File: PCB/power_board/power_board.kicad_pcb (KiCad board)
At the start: 4 copper layers, 70 x 70 mm, 76 parts, among them IC1 TPS6213013AQRGTTQ1, IC10 LSM6DSV16BXTR, IC11 TPS61032PWP, IC7 BQ51013BRHLR, IC8 TPS63000IDRCRQ1, IC9 MAX17048G+T10, J1 Speaker_con, J2 DS1013-40SSIB1-B-0, J8 UJ20-C-H-G-MSMT-R-4C-P16-TR, J9 QVAR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

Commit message: everything checked
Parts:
- added H1: MountingHole, MountingHole:MountingHole_3.2mm_M3_Pad_Via, F.Cu at (32.4, 103.0)
- added H2: MountingHole, MountingHole:MountingHole_3.2mm_M3_Pad_Via, F.Cu at (96.7, 103.5)
- added H3: MountingHole, MountingHole:MountingHole_3.2mm_M3_Pad_Via, F.Cu at (32.6, 167.7)
- added H4: MountingHole, MountingHole:MountingHole_3.2mm_M3_Pad_Via, F.Cu at (97.0, 167.7)
- moved R39 3.66 mm to (30.4, 107.6)
- moved J8 2.58 mm to (44.1, 166.8)
- renumbered indukcja1 to indukcja
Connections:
- D8 pad 4: /USB_D- -> /USB_D-_S
- D8 pad 6: /USB_D+ -> /USB_D+_S
- J2 pad 37: /USB_D+ -> /USB_D+_S
- J2 pad 39: /USB_D- -> /USB_D-_S
- J2 pad 40: unconnected-(J2-Pad40) -> GND
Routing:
- net /USB_D-_S: track 0.00 -> 15.2 mm, vias 0 -> 1
- net /USB_D+_S: track 0.00 -> 15.1 mm
- net /USB_D+: track 29.4 -> 19.0 mm
- net /USB_D-: track 35.6 -> 25.4 mm, vias 3 -> 2
- net GND: track 89.6 -> 93.0 mm
- net Net-(D7-A): track 74.1 -> 77.0 mm
- net Net-(J8-CC1): track 28.4 -> 31.2 mm
- net Net-(J8-CC2): track 11.8 -> 13.7 mm
- net /V_SYS: track 136.9 -> 136.1 mm
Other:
- board size 70 x 70 mm -> 73 x 73 mm

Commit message: all my pcb
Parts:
- removed J8: UJ20-C-H-G-MSMT-R-4C-P16-TR, UJ20-C-H-G-MSMT-R-4C-P16-TR:UJ20CHGMSMTR4CP16TR
- removed J9: QVAR, Connector_JST:JST_PH_B3B-PH-K_1x03_P2.00mm_Vertical
- removed indukcja: Conn_01x02, Connector_PinHeader_2.54mm:PinHeader_1x02_P2.54mm_Vertical
- added J3: USB4110GFA, USB4110GFA:GCT_USB4110GFA, F.Cu at (44.1, 165.2)
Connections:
- net Net-(D7-A) renamed VBUS
- IC10 pad 6: Net-(IC10-AH1/QVAR1) -> unconnected-(IC10-AH1/QVAR1-Pad6)
- IC10 pad 9: Net-(IC10-AH2/QVAR2) -> unconnected-(IC10-AH2/QVAR2-Pad9)
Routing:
- net GND: track 93.0 -> 108.5 mm, vias 33 -> 36
- net Net-(IC10-AH1/QVAR1): track 15.0 -> 0.00 mm, vias 1 -> 0
- net Net-(IC10-AH2/QVAR2): track 9.12 -> 0.00 mm
- net /Movement/WCLK: track 20.4 -> 22.8 mm
- net /USB_D+: track 19.0 -> 21.3 mm
- net VBUS: track 77.0 -> 79.3 mm
- net /USB_D-: track 25.4 -> 27.6 mm
- net /Movement/IMU_INT2: track 14.8 -> 16.8 mm
- net Net-(J3-CC2): track 13.7 -> 14.9 mm
- net Net-(J3-CC1): track 31.2 -> 32.4 mm
- net unconnected-(IC10-AH1/QVAR1-Pad6): track 0.00 -> 0.95 mm, vias 0 -> 1

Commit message: imu from board
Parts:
- removed IC10: LSM6DSV16BXTR, LSM6DSV16BXTR:LSM6DSV16BXTR
- added J4: IMU_connector, Connector_PinHeader_2.54mm:PinHeader_2x05_P2.54mm_Vertical, F.Cu at (73.3, 111.6)
- moved C2 1.35 mm to (78.3, 107.7)
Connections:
- J2 pad 16: /Movement/DATA_IN -> /Movement/SCX
- J2 pad 18: /Movement/BCLK -> /Movement/SDX
- J2 pad 26: /Movement/WCLK -> unconnected-(J2-Pad26)
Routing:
- net /Movement/VOUT_3V3: track 149.9 -> 114.2 mm, vias 3 -> 1
- net /Movement/SDX: track 0.00 -> 24.8 mm
- net /Movement/WCLK: track 22.8 -> 0.00 mm, vias 1 -> 0
- net /Movement/SCX: track 0.00 -> 17.1 mm
- net /Movement/MISO: track 41.8 -> 33.0 mm, vias 3 -> 2
- net /Movement/BCLK: track 8.55 -> 0.00 mm
- net /Movement/DATA_IN: track 7.28 -> 0.00 mm
- net GND: track 108.5 -> 101.9 mm, vias 36 -> 37
- net /Movement/IMU_INT2: track 16.8 -> 10.2 mm, vias 1 -> 0
- net /Movement/MOSI: track 37.6 -> 32.6 mm, vias 3 -> 1
- net /Movement/IMU_CS: track 11.6 -> 8.62 mm, vias 2 -> 0
- net Net-(IC8-VINA): track 23.0 -> 21.7 mm, vias 1 -> 0
- net unconnected-(IC10-AH1/QVAR1-Pad6): track 0.95 -> 0.00 mm, vias 1 -> 0
- net /Movement/SCLK: track 47.3 -> 48.0 mm
- net /Movement/IMU_INT1: track 11.0 -> 11.2 mm, vias 1 -> 0

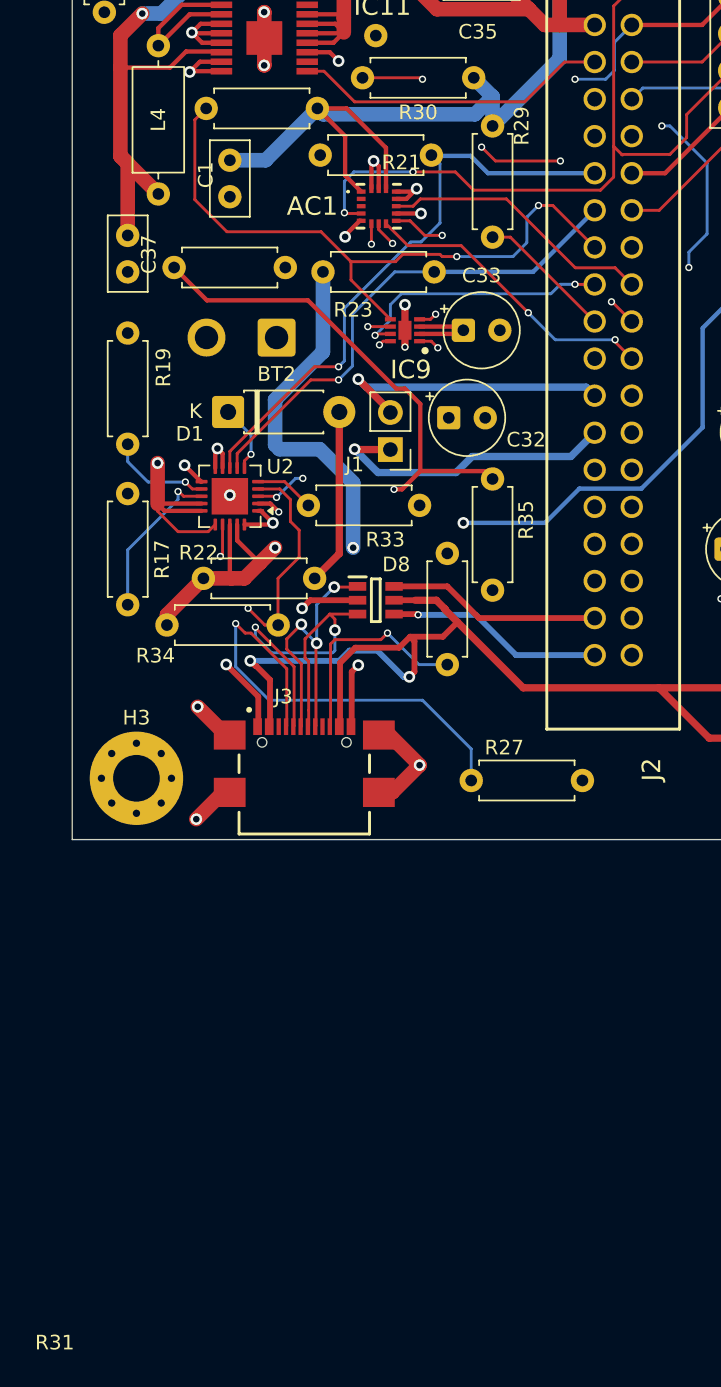
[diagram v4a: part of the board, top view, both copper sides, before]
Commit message: accel changed to goldpin
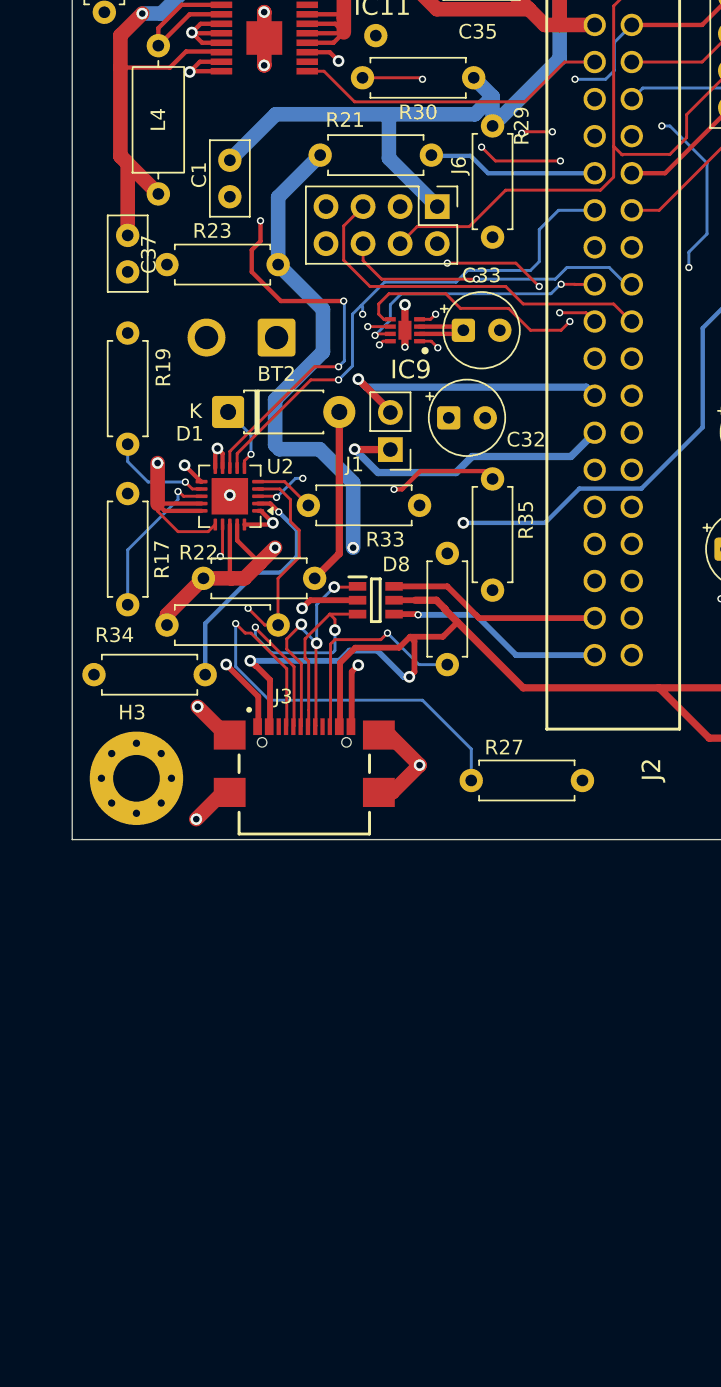
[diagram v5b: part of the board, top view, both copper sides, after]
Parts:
- removed AC1: H3LIS331DLTR, H3LIS331DLTR:LIS3DHTR
- removed R31: 100kΩ, Resistor_THT:R_Axial_DIN0207_L6.3mm_D2.5mm_P7.62mm_Horizontal
- added J6: ACCEL_connector, Connector_PinHeader_2.54mm:PinHeader_2x04_P2.54mm_Vertical, F.Cu at (53.2, 128.5)
- moved R36 28.0 mm to (37.3, 160.6), turned to 180 degrees
- moved R23 18.3 mm to (34.7, 132.5), turned to 0 degrees
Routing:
- net /FG_ALRT: track 44.7 -> 22.1 mm, vias 2 -> 1
- net /STAT2: track 34.5 -> 51.2 mm, vias 1 -> 2
- net /STAT1: track 40.7 -> 54.5 mm, vias 1 -> 3
- net GND: track 101.9 -> 91.4 mm, vias 37 -> 33
- net Net-(U2-VPCC): track 43.3 -> 33.2 mm
- net /Movement/VOUT_3V3: track 114.2 -> 106.0 mm
- net /Movement/ACCEL_CS: track 20.8 -> 27.4 mm
- net /Movement/SCLK: track 48.0 -> 41.6 mm, vias 2 -> 0
- net /Movement/ACCEL_INT2: track 20.7 -> 25.7 mm, vias 2 -> 0
- net /Movement/MOSI: track 32.6 -> 28.3 mm, vias 1 -> 2
- net /Movement/MISO: track 33.0 -> 29.7 mm, vias 2 -> 1
- net /CHARGER_SRC: track 123.0 -> 125.7 mm
- net /Movement/ACCEL_INT1: track 18.8 -> 20.9 mm, vias 0 -> 1
- net /I2C_SDA: track 21.3 -> 22.2 mm, vias 1 -> 2

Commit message: before smd
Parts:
- removed C2: 0.1μF, Capacitor_THT:C_Disc_D5.0mm_W2.5mm_P2.50mm
- removed C3: 10μF, Capacitor_THT:C_Disc_D5.0mm_W2.5mm_P2.50mm
- removed IC8: TPS63000IDRCRQ1, TPS63000IDRCRQ1:TPS63000IDRCRQ1
- removed L1, L3: 2.2µH, Inductor_THT:L_Axial_L7.0mm_D3.3mm_P10.16mm_Horizontal_Fastron_MICC
- removed R26: 1MΩ, Resistor_THT:R_Axial_DIN0207_L6.3mm_D2.5mm_P7.62mm_Horizontal
- removed R28: 180kΩ, Resistor_THT:R_Axial_DIN0207_L6.3mm_D2.5mm_P7.62mm_Horizontal
- removed R37, R41: 10kΩ, Resistor_THT:R_Axial_DIN0207_L6.3mm_D2.5mm_P7.62mm_Horizontal
- removed R38, R42: 100kΩ, Resistor_THT:R_Axial_DIN0207_L6.3mm_D2.5mm_P7.62mm_Horizontal
- removed R39: 200kΩ, Resistor_THT:R_Axial_DIN0207_L6.3mm_D2.5mm_P7.62mm_Horizontal
- removed R40: 750kΩ, Resistor_THT:R_Axial_DIN0207_L6.3mm_D2.5mm_P7.62mm_Horizontal
- added D2: LED, LED_SMD:LED_0603_1608Metric, F.Cu at (94.1, 95.8)
- added L5: 22µH, Inductor_SMD:L_6.3x6.3_H3, F.Cu at (93.3, 76.1)
- added L6: 22µH, Inductor_SMD:L_6.3x6.3_H3, F.Cu at (94.3, 86.4)
- added R1: 1MΩ, Resistor_SMD:R_0603_1608Metric, F.Cu at (90.0, 86.1)
- added R2: 200kΩ, Resistor_SMD:R_0603_1608Metric, F.Cu at (90.0, 88.6)
- added R3: 100kΩ, Resistor_SMD:R_0603_1608Metric, F.Cu at (90.0, 91.1)
- added R31: 100kΩ, Resistor_SMD:R_0603_1608Metric, F.Cu at (81.6, 125.1)
- added R5: 100kΩ, Resistor_SMD:R_0603_1608Metric, F.Cu at (90.0, 93.6)
- added R6: 1kΩ, Resistor_SMD:R_0603_1608Metric, F.Cu at (90.0, 96.1)
- added indukcja1: Conn_01x02, Connector_PinHeader_2.54mm:PinHeader_1x02_P2.54mm_Vertical, F.Cu at (90.6, 128.2)
- C1: value 10μF -> 100μF; footprint Capacitor_THT:C_Disc_D5.0mm_W2.5mm_P2.50mm -> Capacitor_Tantalum_SMD:CP_EIA-3216-18_Kemet-A
- C19, C20, C21, C22, C23, C24, C25, C26, C27, C28, C29, C30, C31, C32, C33: footprint Capacitor_THT:CP_Radial_Tantal_D5.0mm_P2.50mm -> Capacitor_Tantalum_SMD:CP_EIA-3216-18_Kemet-A
- C34, C35, C37, C4: footprint Capacitor_THT:C_Disc_D5.0mm_W2.5mm_P2.50mm -> Capacitor_SMD:CP_Elec_6.3x5.4
- C5: value 10µF -> 10μF; footprint Capacitor_THT:C_Disc_D5.0mm_W2.5mm_P2.50mm -> Capacitor_SMD:CP_Elec_6.3x5.4
- C6: value 10µF -> 10u X7R; footprint Capacitor_THT:C_Disc_D5.0mm_W2.5mm_P2.50mm -> Capacitor_SMD:CP_Elec_6.3x5.4
- D1, D6: footprint Diode_THT:D_DO-41_SOD81_P7.62mm_Horizontal -> LED_SMD:LED_0603_1608Metric
- IC1: value TPS6213013AQRGTTQ1 -> TPS61131PW; footprint TPS6213013AQRGTTQ1:QFN50P300X300X100-17N-D -> TPS61131PW:SOP65P640X120-16N
- L4: footprint Inductor_THT:L_Axial_L7.0mm_D3.3mm_P10.16mm_Horizontal_Fastron_MICC -> Inductor_SMD:L_6.3x6.3_H3
- R17, R18, R19, R20, R21, R22, R23, R24, R25, R27, R29, R30, R32, R33, R34, R35, R36, TH4: footprint Resistor_THT:R_Axial_DIN0207_L6.3mm_D2.5mm_P7.62mm_Horizontal -> Resistor_SMD:R_0603_1608Metric
- moved C5 20.5 mm to (80.0, 103.1)
- moved R32 9.52 mm to (57.3, 168.8), turned to -90 degrees
- moved C37 7.82 mm to (31.5, 138.3)
- moved R35 6.15 mm to (51.7, 151.7)
- moved C4 5.78 mm to (34.2, 112.3)
- moved C31 3.21 mm to (76.8, 128.3)
- moved C35 2.97 mm to (53.0, 110.8)
- moved C6 2.60 mm to (53.4, 102.0), turned to 0 degrees
- moved L4 2.46 mm to (34.0, 125.2)
- moved R27 2.38 mm to (53.4, 168.9), turned to -90 degrees
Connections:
- C1 pad 1: GND -> /Movement/VOUT_3V3
- C1 pad 2: /Movement/VOUT_3V3 -> GND
- C5 pad 1: GND -> /V_SYS
- C5 pad 2: /STEP_UP/OUT+5V -> GND
- C6 pad 1: GND -> Net-(IC1-SWP)
- C6 pad 2: Net-(IC1-SS/TR) -> Net-(IC1-SWN)
- IC1 pad 1: Net-(IC1-SW_1) -> Net-(IC1-SWP)
- IC1 pad 10: /STEP_UP/OUT+5V -> GND
- IC1 pad 11: /STEP_UP/OUT+5V -> GND
- IC1 pad 12: /STEP_UP/OUT+5V -> GND
- IC1 pad 14: /3V8 -> Net-(IC1-PGOOD)
- IC1 pad 16: GND -> /Movement/VOUT_3V3
- IC1 pad 2: Net-(IC1-SW_1) -> Net-(IC1-SWN)
- IC1 pad 3: Net-(IC1-SW_1) -> GND
- IC1 pad 4: Net-(IC1-PG) -> /V_SYS
- IC1 pad 7: GND -> /V_SYS
- IC1 pad 8: GND -> /V_SYS
- IC1 pad 9: Net-(IC1-SS/TR) -> GND
- J2 pad 2: /3V8 -> unconnected-(J2-Pad2)
- J3 pad B6: /USB_D+ -> unconnected-(J3-DP2-PadB6)
- J3 pad B7: /USB_D- -> unconnected-(J3-DN2-PadB7)
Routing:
- net (no net): track 0.00 -> 92.1 mm, vias 0 -> 3
- net unconnected-(J2-Pad2): track 0.00 -> 51.2 mm, vias 0 -> 1
- net /3V8: track 51.2 -> 0.00 mm, vias 1 -> 0
- net GND: track 91.4 -> 130.2 mm, vias 33 -> 37
- net Net-(IC1-LBI): track 28.3 -> 0.00 mm, vias 1 -> 0
- net Net-(IC8-VINA): track 21.7 -> 0.00 mm
- net Net-(J3-CC1): track 32.4 -> 12.9 mm, vias 1 -> 0
- net Net-(IC1-SW_1): track 19.2 -> 0.00 mm
- net /FG_ALRT: track 22.1 -> 41.2 mm
- net Net-(IC8-L2): track 18.6 -> 0.00 mm, vias 1 -> 0
- net /USB_D-: track 27.6 -> 10.2 mm, vias 2 -> 0
- net /Movement/VOUT_3V3: track 106.0 -> 121.8 mm
- net Net-(IC8-FB): track 14.4 -> 0.00 mm
- net /STEP_UP/OUT+5V: track 76.2 -> 61.9 mm
- net Net-(IC1-SWP): track 0.00 -> 12.8 mm, vias 0 -> 2
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
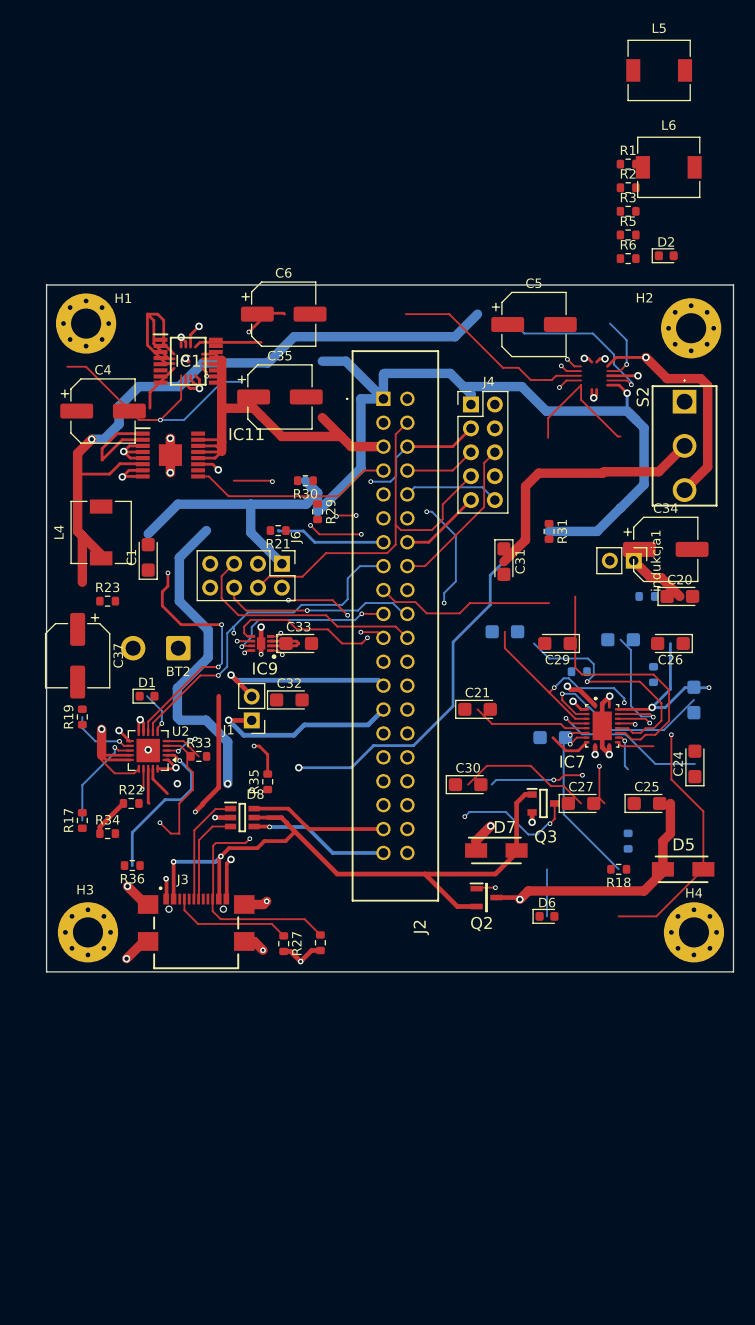
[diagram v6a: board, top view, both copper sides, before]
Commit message: goldpins on one side
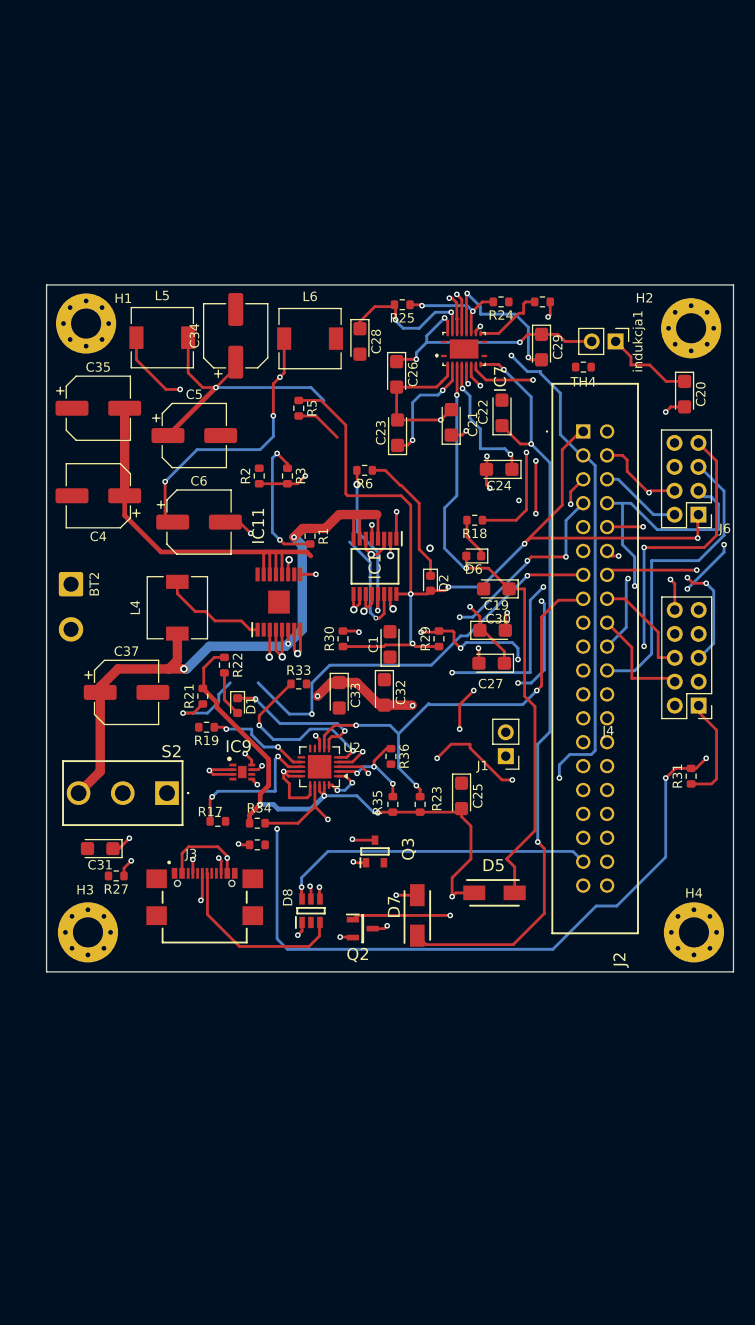
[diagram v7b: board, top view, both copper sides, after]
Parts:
- C19, C22, C23, C28, R20, R24, R25, TH4: moved to F.Cu
- moved S2 69.0 mm to (41.0, 152.9), turned to 180 degrees
- moved L5 60.0 mm to (40.5, 104.5)
- moved C31 52.6 mm to (33.9, 158.8), turned to 180 degrees
- moved R1 52.0 mm to (56.2, 125.6), turned to -90 degrees
- moved C34 51.0 mm to (48.3, 104.3), turned to 90 degrees
- moved TH4 50.6 mm to (85.2, 107.6), turned to 180 degrees
- moved R2 49.8 mm to (50.8, 119.2), turned to 90 degrees
- moved R3 45.8 mm to (53.8, 119.2), turned to -90 degrees
- moved J6 44.6 mm to (97.5, 123.3), turned to 180 degrees
- moved R25 43.3 mm to (66.0, 101.0)
- moved D2 42.9 mm to (69.0, 130.6), turned to -90 degrees
- moved IC7 42.4 mm to (72.2, 105.7), turned to 90 degrees
- moved C23 42.4 mm to (65.5, 114.6)
- moved L6 42.2 mm to (56.2, 104.6)
- moved C28 42.1 mm to (61.5, 104.9), turned to -90 degrees
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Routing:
- net GND: track 130.2 -> 29.9 mm, vias 37 -> 8
- net (no net): track 92.1 -> 0.00 mm, vias 3 -> 0
- net Net-(IC7-~{AD-EN}): track 23.3 -> 90.3 mm, vias 2 -> 6
- net /FG_ALRT: track 41.2 -> 104.3 mm, vias 1 -> 4
- net /USB_SRC: track 19.9 -> 82.5 mm, vias 1 -> 3
- net Net-(IC1-SWN): track 0.00 -> 52.0 mm, vias 0 -> 3
- net unconnected-(J2-Pad2): track 51.2 -> 0.00 mm, vias 1 -> 0
- net /CHARGER_SRC: track 119.9 -> 71.6 mm, vias 3 -> 5
- net Net-(IC1-SWP): track 12.8 -> 56.3 mm, vias 2 -> 4
- net Net-(S2-COM): track 80.7 -> 38.1 mm, vias 2 -> 3
- net /I2C_SDA: track 22.2 -> 64.8 mm, vias 2 -> 6
- net /V_SYS: track 141.4 -> 99.9 mm, vias 2 -> 4
- net Net-(IC7-CLAMP2): track 12.7 -> 48.7 mm
- net Net-(Q3-D): track 48.8 -> 13.9 mm, vias 4 -> 2
- net /BAT+: track 65.1 -> 95.6 mm, vias 1 -> 4
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
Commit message: modified gnd
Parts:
- C19, C22, C23, C28, R20, R24, R25, TH4: moved to B.Cu
- moved S2 69.0 mm to (96.0, 111.3), turned to -90 degrees
- moved L5 60.0 mm to (93.3, 76.1)
- moved C31 52.6 mm to (76.8, 128.3), turned to -90 degrees
- moved R1 52.0 mm to (90.0, 86.1), turned to 0 degrees
- moved C34 51.0 mm to (94.0, 127.0), turned to 0 degrees
- moved TH4 50.6 mm to (90.0, 158.0), turned to 90 degrees
- moved R2 49.8 mm to (90.0, 88.6), turned to 0 degrees
- moved R3 45.8 mm to (90.0, 91.1), turned to 0 degrees
- moved J6 44.6 mm to (53.2, 128.5), turned to -90 degrees
- moved R25 43.3 mm to (84.8, 140.0)
- moved D2 42.9 mm to (94.1, 95.8), turned to 0 degrees
- moved IC7 42.4 mm to (87.2, 145.4), turned to 0 degrees
- moved C23 42.4 mm to (97.0, 143.0)
- moved L6 42.2 mm to (94.3, 86.4)
- moved C28 42.1 mm to (89.2, 136.6), turned to 180 degrees
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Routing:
- net GND: track 29.9 -> 130.2 mm, vias 8 -> 37
- net (no net): track 0.00 -> 92.1 mm, vias 0 -> 3
- net Net-(IC7-~{AD-EN}): track 90.3 -> 23.3 mm, vias 6 -> 2
- net /FG_ALRT: track 104.3 -> 41.2 mm, vias 4 -> 1
- net /USB_SRC: track 82.5 -> 19.9 mm, vias 3 -> 1
- net Net-(IC1-SWN): track 52.0 -> 0.00 mm, vias 3 -> 0
- net unconnected-(J2-Pad2): track 0.00 -> 51.2 mm, vias 0 -> 1
- net /CHARGER_SRC: track 71.6 -> 119.9 mm, vias 5 -> 3
- net Net-(IC1-SWP): track 56.3 -> 12.8 mm, vias 4 -> 2
- net Net-(S2-COM): track 38.1 -> 80.7 mm, vias 3 -> 2
- net /I2C_SDA: track 64.8 -> 22.2 mm, vias 6 -> 2
- net /V_SYS: track 99.9 -> 141.4 mm, vias 4 -> 2
- net Net-(IC7-CLAMP2): track 48.7 -> 12.7 mm
- net Net-(Q3-D): track 13.9 -> 48.8 mm, vias 2 -> 4
- net /BAT+: track 95.6 -> 65.1 mm, vias 4 -> 1
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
